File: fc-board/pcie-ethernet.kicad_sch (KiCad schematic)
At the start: 55 parts, among them J15 Conn_01x04_Pin, U11 LAN7430T-I/Y9X, Y1 DSC1001CI2-025.0000T

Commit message: Finished routing; cleaned library
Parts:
- removed R42, R43: 0, Resistor_SMD:R_0805_2012Metric, symbol Device:R_Small
- removed TP10: TXCM, fc-board:TestPoint_THTPad_D2.0mm_Drill1.0mm_JLCrules, symbol Connector:TestPoint
- removed TP11: TXPC, fc-board:TestPoint_THTPad_D2.0mm_Drill1.0mm_JLCrules, symbol Connector:TestPoint
- added JP17: TEST_3V3, Jumper:SolderJumper-2_P1.3mm_Open_Pad1.0x1.5mm, symbol Jumper:SolderJumper_2_Open
- added JP18: TEST_GND, Jumper:SolderJumper-2_P1.3mm_Open_Pad1.0x1.5mm, symbol Jumper:SolderJumper_2_Open
- renumbered C25 to C27, C26 to C28, C27 to C29, C28 to C30, C29 to C31, C30 to C32, C31 to C33, C32 to C34, C33 to C35, C34 to C36, C35 to C37, C36 to C38, C37 to C39, C38 to C40, C39 to C41, C40 to C42, C41 to C43, C42 to C44, C43 to C45, C44 to C46, C45 to C47, C46 to C48, C47 to C49, C48 to C50, C49 to C51, C50 to C52, C51 to C53, C52 to C54, J15 to J16, JP7 to JP19, R40 to R39, R41 to R40, R44 to R41, R45 to R42, R46 to R43, R47 to R44, TP9 to TP15, TP12 to TP16, TP13 to TP17, TP14 to TP18
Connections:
- net 3.3V: now also JP17.2 (B)
- net GND: now also JP18.1 (A)
- net at U11.30 (TEST): now also JP17.1 (A), JP18.2 (B)
- net PCIE_CLK_M renamed PCIE_CLK_N
- net PCIE_RX_M renamed PCIE_RX_N
- net PCIE_TX_M renamed PCIE_TX_N
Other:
- note added: "Might not need this; need to confirm after ordering the first version of this board."
- title: (none) -> PCIE-to-ethernet interface
- moved on the sheet: FB1, FB2, FB3, FB4, FB5

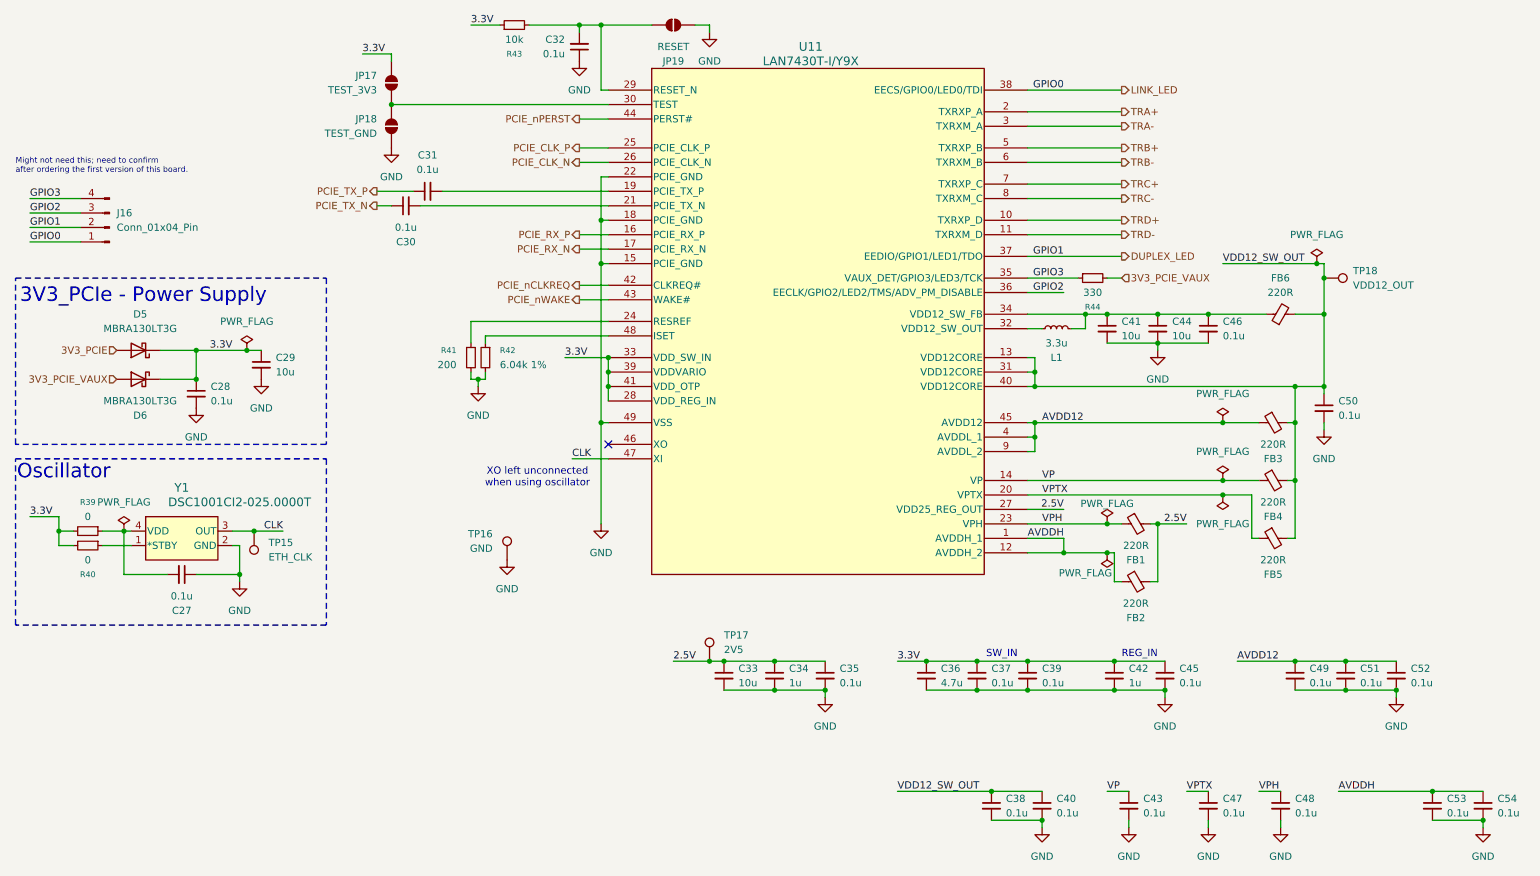
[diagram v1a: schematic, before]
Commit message: Updated RJ45 jack
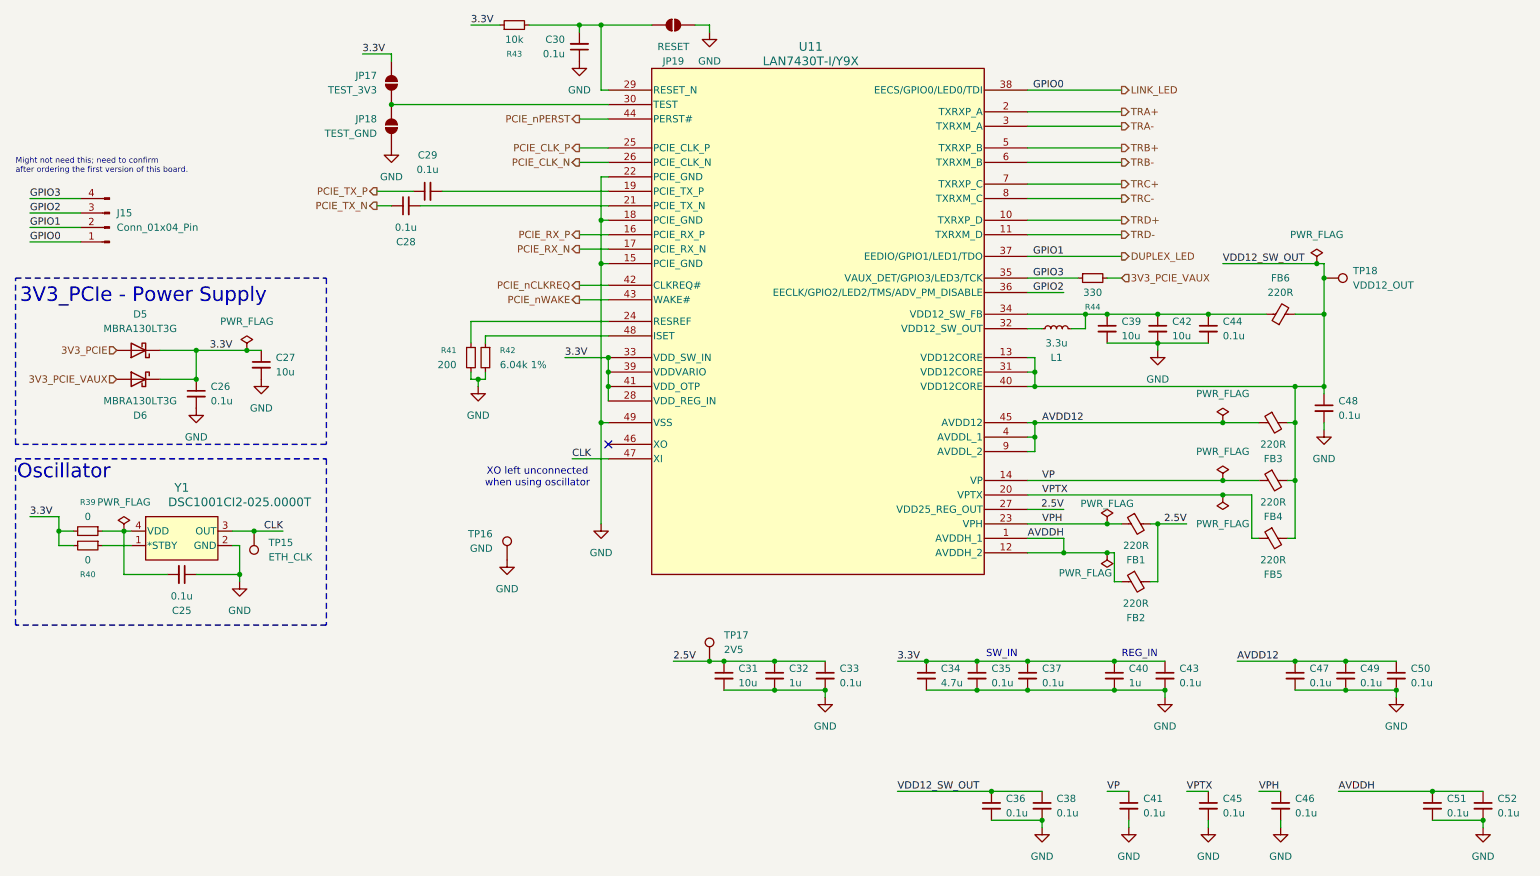
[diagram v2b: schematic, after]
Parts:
- renumbered C27 to C25, C28 to C26, C29 to C27, C30 to C28, C31 to C29, C32 to C30, C33 to C31, C34 to C32, C35 to C33, C36 to C34, C37 to C35, C38 to C36, C39 to C37, C40 to C38, C41 to C39, C42 to C40, C43 to C41, C44 to C42, C45 to C43, C46 to C44, C47 to C45, C48 to C46, C49 to C47, C50 to C48, C51 to C49, C52 to C50, C53 to C51, C54 to C52, J16 to J15

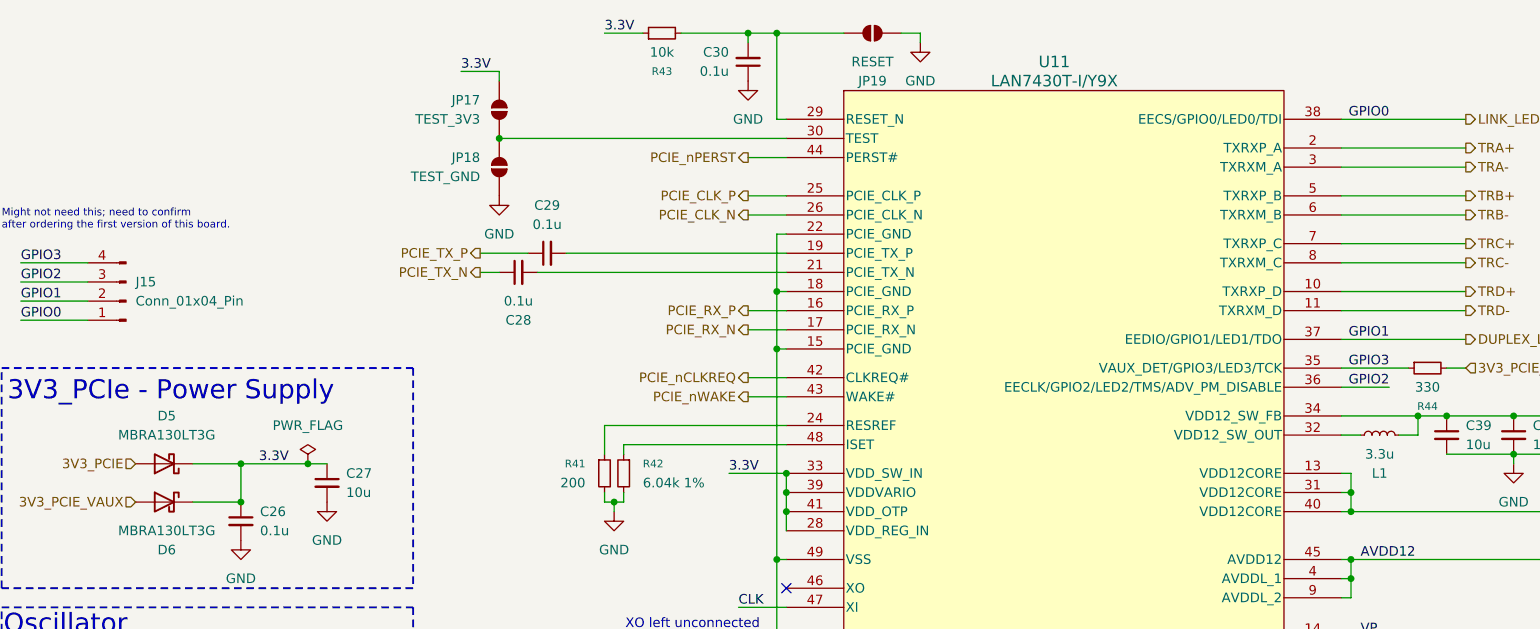
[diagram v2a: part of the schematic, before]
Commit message: Assigned part numbers to everything, replaced ethernet jack
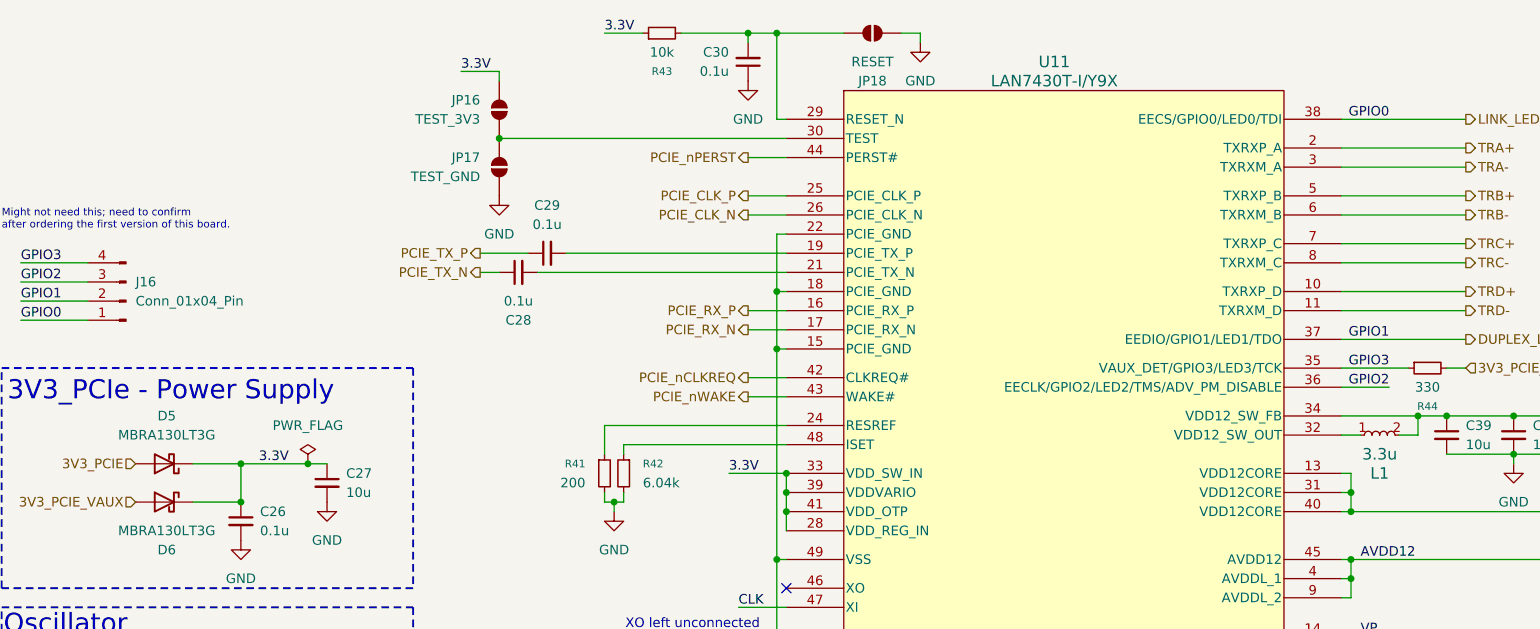
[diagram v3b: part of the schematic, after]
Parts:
- removed L1: 3.3u, Inductor_SMD:L_0805_2012Metric, symbol Device:L_Small
- added L1: 3.3u, fc-board:VLS3012HBX-3R3M, symbol fc-board:VLS3012HBX-3R3M
- R42: value 6.04k 1% -> 6.04k
- renumbered J15 to J16, JP17 to JP16, JP18 to JP17, JP19 to JP18
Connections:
- net at C39.1, C42.1, C44.1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: now also L1.2
- net at U11.32 (VDD12_SW_OUT): now also L1.1

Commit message: fix stupid merge issue
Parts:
- J16: now not fitted
- TP13: renamed from TP15; symbol Connector:TestPoint -> fc-board:TestPoint; now left out of the parts list
- TP14: renamed from TP16; symbol Connector:TestPoint -> fc-board:TestPoint; now left out of the parts list
- TP15: renamed from TP17; symbol Connector:TestPoint -> fc-board:TestPoint; now left out of the parts list
- TP16: renamed from TP18; symbol Connector:TestPoint -> fc-board:TestPoint; now left out of the parts list
- renumbered JP16 to JP19, JP17 to JP20, JP18 to JP21, R39 to R38, R40 to R39, R41 to R40, R42 to R41, R43 to R42, R44 to R43, U11 to U8
